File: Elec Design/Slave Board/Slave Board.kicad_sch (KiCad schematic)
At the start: 83 parts, among them J6 0022232041, J7 Conn_ARM_JTAG_SWD_10, M1 VID28-05, M2 VID28-05, M3 VID28-05, M4 VID28-05, SW1 SW_SPST, U1 LPC11C24-LQFP48, U10 DRV5033AJxDBZ, U11 DRV5033AJxDBZ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

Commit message: further bom alignment
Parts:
- removed SW1: SW_SPST, Switches:SW_SPST_ SKRPASE010, symbol Switch:SW_MEC_5E
- added SW1: SW_SPST, Button_Switch_SMD:SW_SPST_PTS810, symbol Switch:SW_SPST
- C1, C10, C11, C12, C13, C16, C18, C19, C2, C21, C22, C23, C24, C3, C4, C5, C6, C7, C8, C9: footprint Capacitor_SMD:C_0805_2012Metric_Pad1.18x1.45mm_HandSolder -> Capacitor_SMD:C_0603_1608Metric
- C26: JLC PN (none) -> C2244191; JLC? N -> (none); MPN C0603C104K5RECAUTO -> GRM188R6YA106MA73J; Rated V 50V -> 35V
- C27, C28: value 0.1uF -> 100nF
- C30, C31: JLC PN (none) -> C2992620
- D5: JLC PN (none) -> C64982; JLC? N -> (none)
- J3, J5: footprint digikey-footprints:Term_Block_1x3_P5mm -> TerminalBlock_Phoenix:TerminalBlock_Phoenix_PT-1,5-3-5.0-H_1x03_P5.00mm_Horizontal
- J6: value 0022232041 -> ~; footprint digikey-footprints:PinHeader_1x4_P2.54mm_Drill1.02mm -> Connector_PinHeader_2.54mm:PinHeader_1x04_P2.54mm_Vertical; Category Connectors, Interconnects -> (none); DK_Datasheet_Link https://www.molex.com/pdm_docs/sd/022232041_sd.pdf -> (none); DK_Detail_Page /product-detail/en/molex/0022232041/WM4202-ND/26671 -> https://www.digikey.ca/en/products/detail/würth-elektronik/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; Digi-Key_PN WM4202-ND -> 732-5317-ND; Family Rectangular Connectors - Headers, Male Pins -> (none); MPN 0022232041 -> 61300411121; Manufacturer Molex -> (none); Status Active -> (none)
- J7: footprint 10 pin jtag:CONN_3220-10-0100-00_CNC -> digikey-footprints:PinHeader_2x5_P1.27mm_Drill.7mm
- J8, J9: footprint digikey-footprints:Terminal_Block_D1.3mm_P5mm -> TerminalBlock_Phoenix:TerminalBlock_Phoenix_PT-1,5-2-5.0-H_1x02_P5.00mm_Horizontal
- L1: footprint NR6028T4R7M:IND_NR6028T4R7M -> Inductors:IND_NR6028T4R7M
- R10, R11, R12, R13, R17, R18, R20, R29, R30, R5, R6, R7, R8, R9: footprint Resistor_SMD:R_0805_2012Metric_Pad1.20x1.40mm_HandSolder -> Resistor_SMD:R_0603_1608Metric
- R22: footprint Resistor_SMD:R_1206_3216Metric_Pad1.30x1.75mm_HandSolder -> Resistor_SMD:R_0603_1608Metric
- U1: JLC PN (none) -> C1020252; MPN (none) -> LPC11C24FBD48
- U14: footprint HTSOP-J8_ROM -> Buck Converter:HTSOP-J8_ROM
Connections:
- net GND: now also SW1.2 (B)
- net at R20.2: now also SW1.1 (A)
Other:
- moved on the sheet: C18, R18, R20, Y1

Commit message: minor bom changes
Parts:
- D5: MPN B340AE -> C64982
- J3, J5: JLC PN (none) -> C3816891
- J8, J9: JLC PN (none) -> C3819953
- L1: JLC PN (none) -> C77758
- SW1: MPN PTS810SJS250SMTRLFS -> C221897
- U1: MPN LPC11C24FBD48 -> C1020252
- U14: JLC PN (none) -> C919448; MPN (none) -> C919448
- U15: MPN (none) -> C2891841
- Y1: JLC PN (none) -> C2975357; MPN (none) -> C2975357
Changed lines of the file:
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@@
 			)
 		)
+		(property "JLC PN" "C77758"
+			(at 267.97 45.72 0)
+			(effects
+				(font
+					(size 1.27 1.27)
+				)
+				(hide yes)
+			)
+		)
 		(pin "1"
 		)
@@
 			)
 		)
-		(property "Datasheet" "https://www.diodes.com/assets/Datasheets/B320AE/B340AE.pdf"
+		(property "Datasheet" "https://www.lcsc.com/datasheet/lcsc_datasheet_2307101649_MDD-Microdiode-Electronics-B340A_C64982.pdf"
 			(at 147.32 48.26 0)
 			(effects
@@
 			)
 		)
-		(property "MPN" "B340AE"
+		(property "MPN" "C64982"
 			(at 147.32 48.26 0)
 			(effects
@@
 			)
 		)
+		(property "MPN" "C2891841"
+			(at 347.98 48.26 0)
+			(effects
+				(font
+					(size 1.27 1.27)
+				)
+				(hide yes)
+			)
+		)
 		(pin "1"
 		)
@@
 			)
 		)
+		(property "JLC PN" "C3816891"
+			(at 127 316.23 0)
+			(effects
+				(font
+					(size 1.27 1.27)
+				)
+				(hide yes)
+			)
+		)
 		(pin "1"
 		)
@@
 			)
 		)
+		(property "JLC PN" "C3816891"
+			(at 153.67 339.09 0)
+			(effects
+				(font
+					(size 1.27 1.27)
+				)
+				(hide yes)
+			)
+		)
 		(pin "1"
 		)
@@
 			)
 		)
+		(property "JLC PN" "C2975357"
+			(at 119.38 238.76 0)
+			(effects
+				(font
+					(size 1.27 1.27)
+				)
+				(hide yes)
+			)
+		)
+		(property "MPN" "C2975357"
+			(at 119.38 238.76 0)
+			(effects
+				(font
+					(size 1.27 1.27)
+				)
+				(hide yes)
+			)
+		)
 		(pin "1"
 		)
@@
 			)
 		)
+		(property "JLC PN" "C3819953"
+			(at 95.885 48.26 0)
+			(effects
+				(font
+					(size 1.27 1.27)
+				)
+				(hide yes)
+			)
+		)
 		(pin "1"
 		)
@@
 			)
 		)
+		(property "MPN" "C919448"
+			(at 192.405 45.72 0)
+			(effects
+				(font
+					(size 1.27 1.27)
+				)
+				(hide yes)
+			)
+		)
+		(property "JLC PN" "C919448"
+			(at 192.405 45.72 0)
+			(effects
+				(font
+					(size 1.27 1.27)
+				)
+				(hide yes)
+			)
+		)
 		(pin "1"
 		)
@@
 			)
 		)
-		(property "MPN" "LPC11C24FBD48"
+		(property "MPN" "C1020252"
 			(at 165.1 240.03 0)
 			(effects
@@
 			)
 		)
-		(property "MPN" "PTS810SJS250SMTRLFS"
+		(property "MPN" "C221897"
 			(at 240.03 119.38 0)
 			(effects
@@
 				(hide yes)
 			)
+		)
+		(property "JLC PN" "C3819953"
+			(at 120.015 34.29 0)
+			(effects
+				(font
+					(size 1.27 1.27)
+				)
+				(hide yes)
+			)

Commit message: bom ordering
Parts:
- J3: value ~ -> 1935174
- J6: value ~ -> 61300411121
- J8, J9: value ~ -> 1935161
- U15: MPN C2891841 -> C603785
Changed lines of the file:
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@@
 			)
 		)
-		(property "MPN" "C2891841"
+		(property "MPN" "C603785"
 			(at 347.98 48.26 0)
 			(effects
@@
 			)
 		)
-		(property "Value" "~"
+		(property "Value" "1935174"
 			(at 127.635 312.42 90)
 			(effects
@@
 			)
 		)
-		(property "Value" "~"
+		(property "Value" "61300411121"
 			(at 402.59 40.6399 90)
 			(effects
@@
 			)
 		)
-		(property "Value" "~"
+		(property "Value" "1935161"
 			(at 96.52 44.45 90)
 			(effects
@@
 			)
 		)
-		(property "Value" "~"
+		(property "Value" "1935161"
 			(at 117.475 36.1949 0)
 			(effects

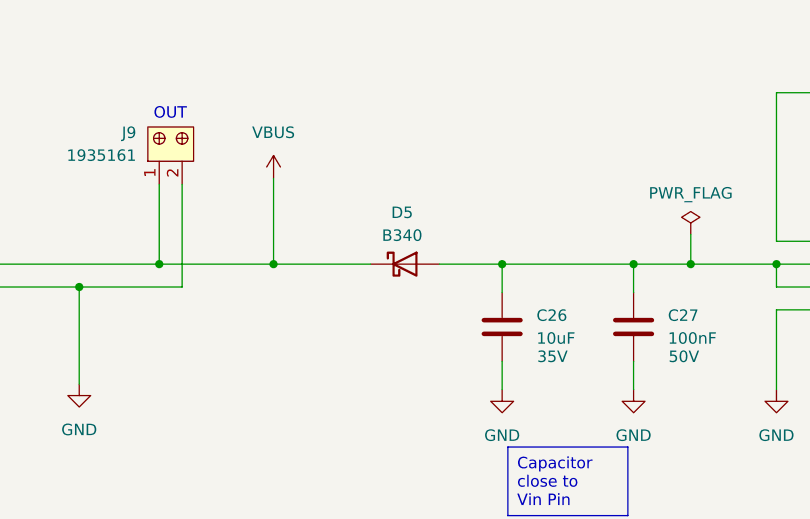
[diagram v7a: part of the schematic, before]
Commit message: corrected barrier diode direction on both boards
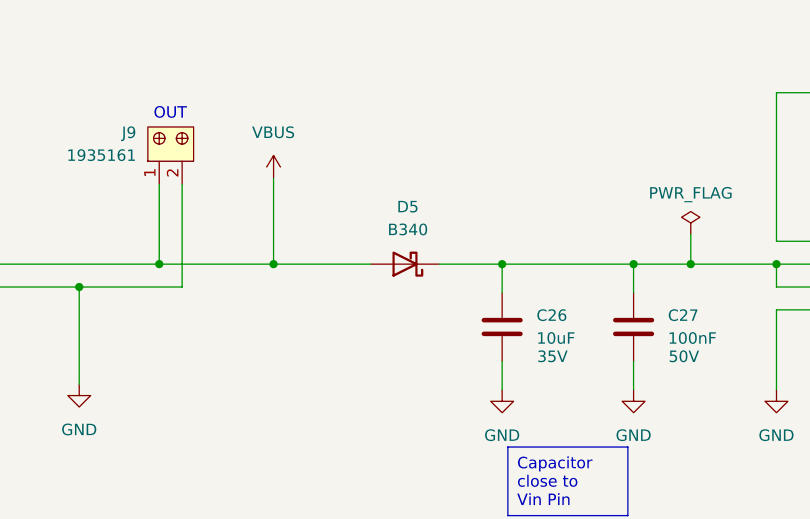
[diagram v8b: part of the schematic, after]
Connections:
- net VBUS: now also D5.2 (A); no longer D5.1 (K)
- net at C26.1, C27.1, U14.2 (VIN)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: now also D5.1 (K); no longer D5.2 (A)
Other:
- moved on the sheet: D5
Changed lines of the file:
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@@
 	(symbol
 		(lib_id "Diode:B340")
-		(at 147.32 48.26 0)
+		(at 147.32 48.26 180)
 		(unit 1)
 		(exclude_from_sim no)
@@
 		(fields_autoplaced yes)
 		(property "Reference" "D5"
-			(at 147.0025 42.545 0)
+			(at 147.6375 41.91 0)
 			(effects
 				(font
@@
 		)
 		(property "Value" "B340"
-			(at 147.0025 45.085 0)
+			(at 147.6375 44.45 0)
 			(effects
 				(font
@@
 		)
 		(property "Footprint" "Diode_SMD:D_SMA"
-			(at 147.32 52.705 0)
+			(at 147.32 43.815 0)
 			(effects
 				(font
